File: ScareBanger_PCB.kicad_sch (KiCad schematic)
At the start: 15 parts, among them J1 RJ45, J16 Conn_01x10_Female - SAINSMART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, J17 Screw_Terminal_01x10 - HILETG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, J2 1757271, J3 Screw_Terminal_01x06, J4 Barrel_Jack_Switch, J6 Screw_Terminal_01x06, J7 Screw_Terminal_01x06, SW1 SW_SPDT, SW2 SW_SPDT

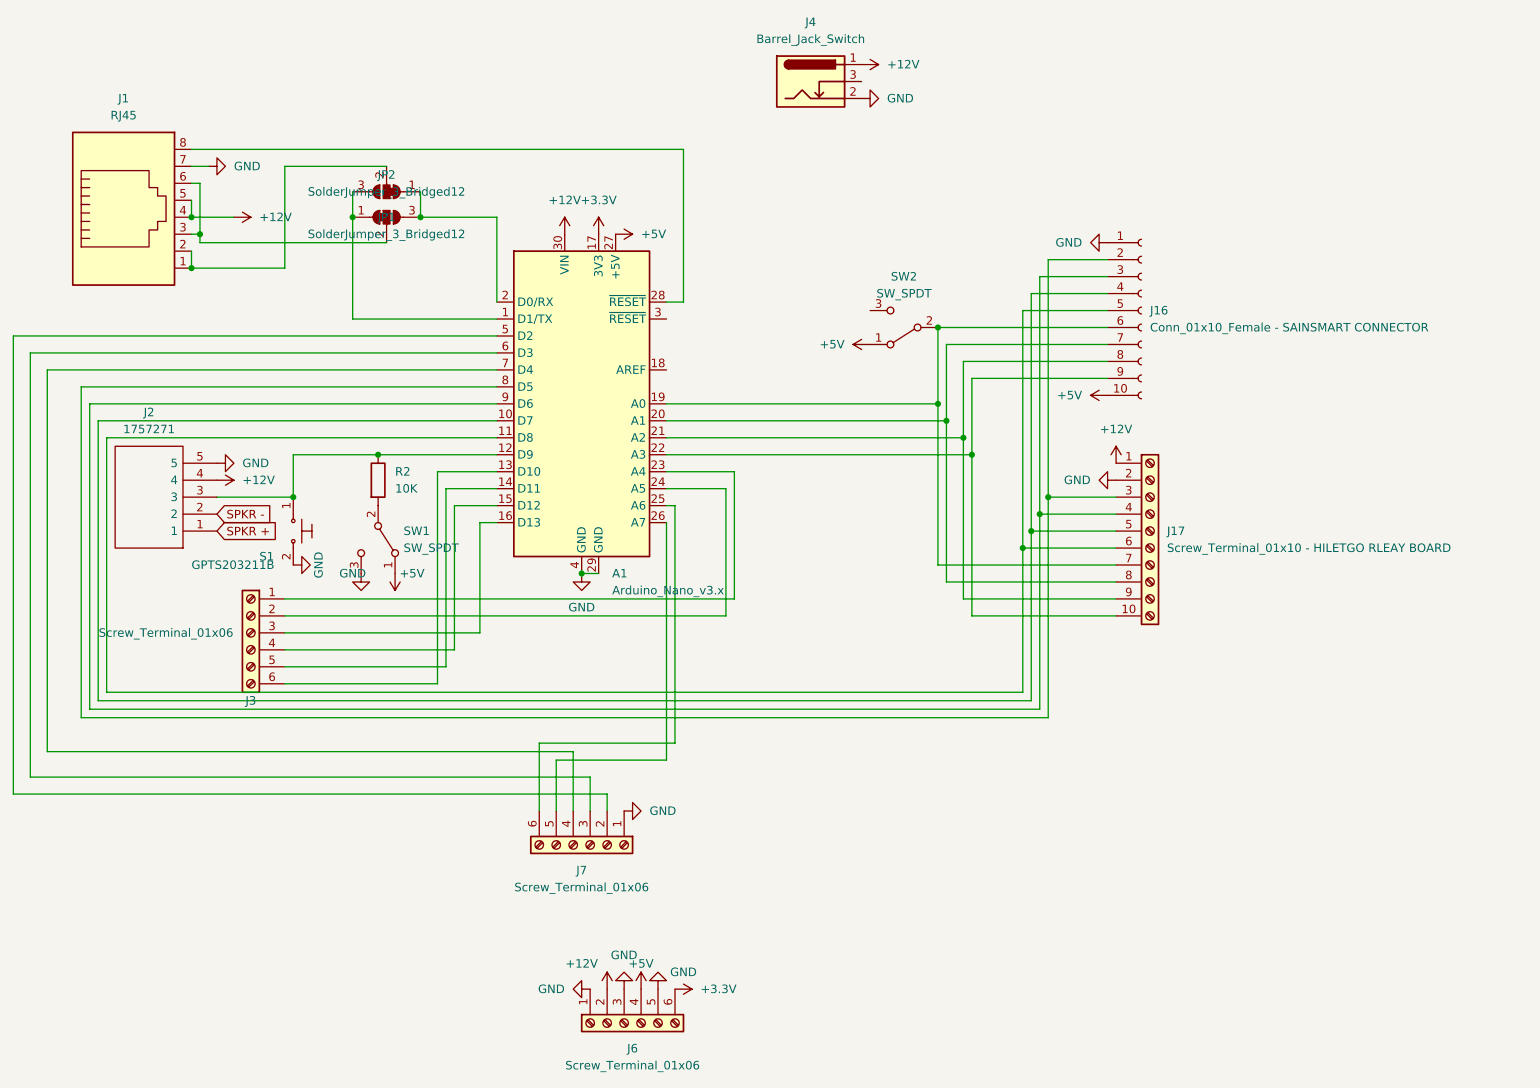
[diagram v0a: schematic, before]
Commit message: Trigger pin changed to D4
trigger pin switched from D9 to D4 so D9 with its PWM is available for outputs
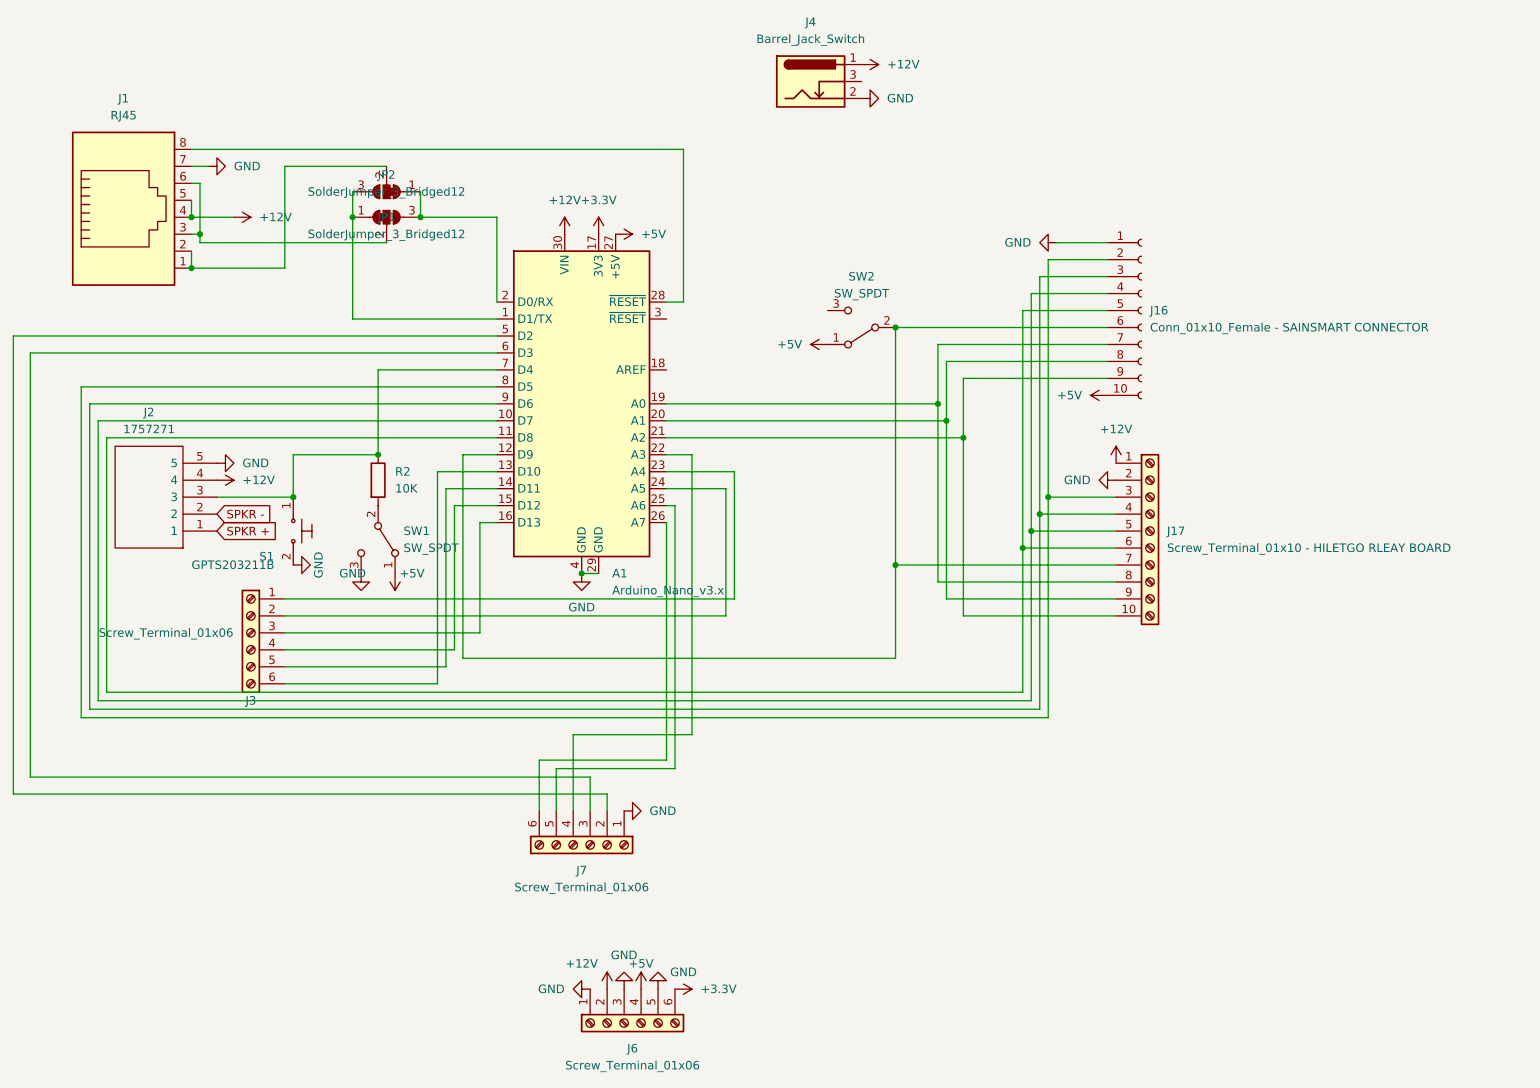
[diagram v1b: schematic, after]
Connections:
- net at J2.3, R2.1, S1.1: now also A1.7 (D4); no longer A1.12 (D9)
- net at J16.6 (Pin_6), J17.7 (Pin_7), SW2.2 (B): now also A1.12 (D9); no longer A1.19 (A0)
- net at J16.7 (Pin_7), J17.8 (Pin_8): now also A1.19 (A0); no longer A1.20 (A1)
- net at J16.8 (Pin_8), J17.9 (Pin_9): now also A1.20 (A1); no longer A1.21 (A2)
- net at J16.9 (Pin_9), J17.10 (Pin_10): now also A1.21 (A2); no longer A1.22 (A3)
- net at J7.4 (Pin_4): now also A1.22 (A3); no longer A1.7 (D4)
- net at J7.5 (Pin_5): now also A1.25 (A6); no longer A1.26 (A7)
- net at J7.6 (Pin_6): now also A1.26 (A7); no longer A1.25 (A6)
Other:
- moved on the sheet: SW2
